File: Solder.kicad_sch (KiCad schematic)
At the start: 83 parts, among them K1 SRD-24VDC-SL-C, U1 5082-7610, U2 5082-7610, U3 5082-7610, X1 1x07F, X2 1x07F, X3 1x07F, X4 1x02, X5 1x04, X6 01x02F

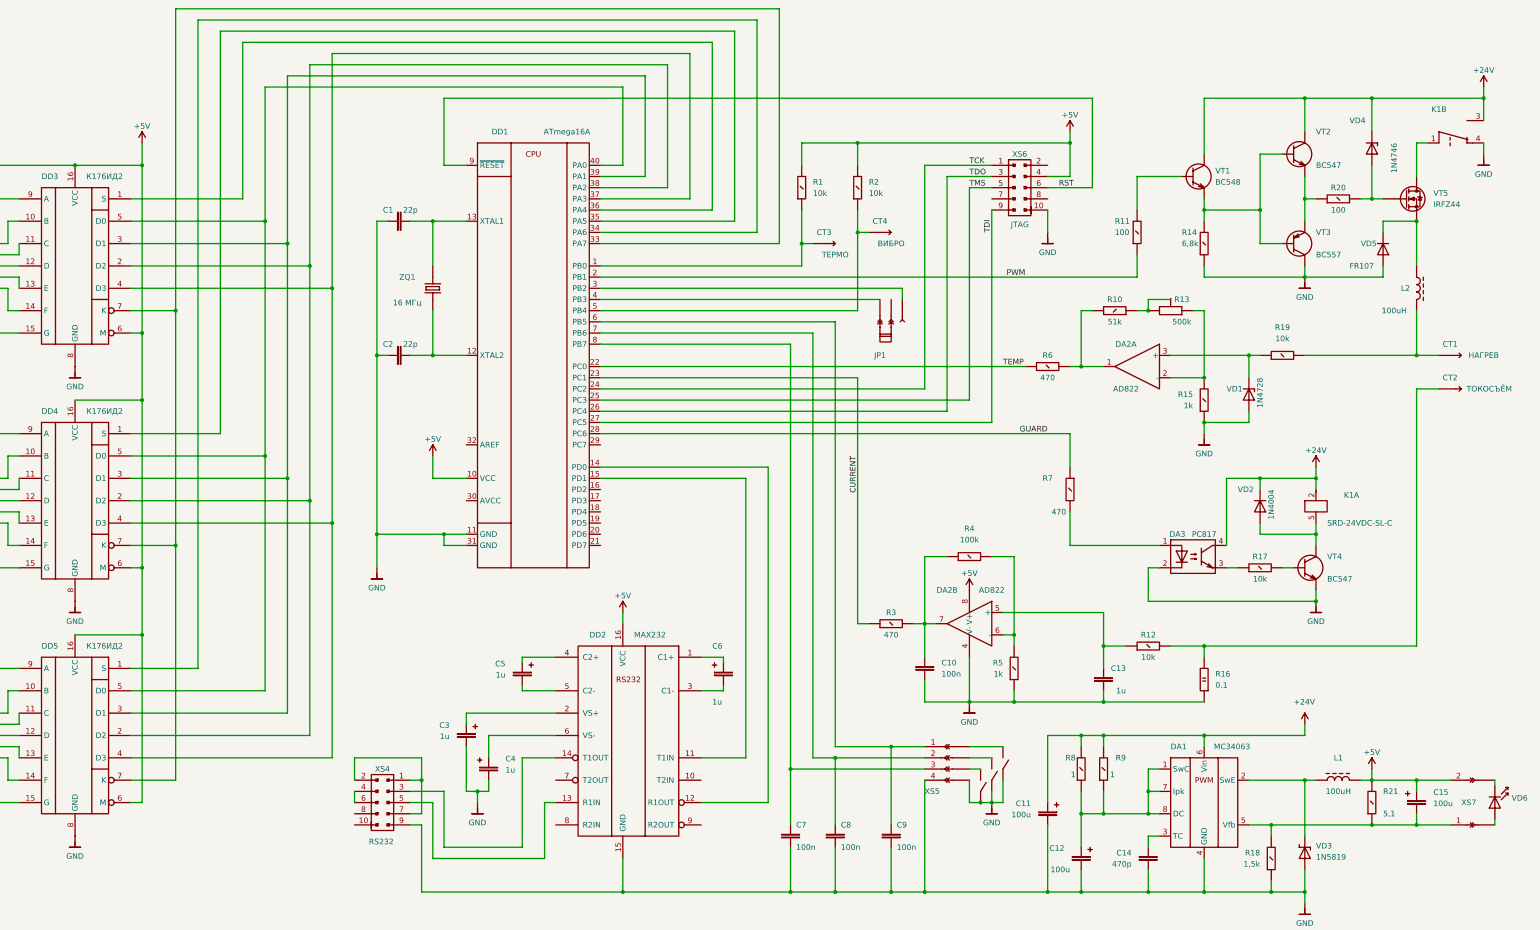
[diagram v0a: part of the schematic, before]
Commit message: Fixed schematic errors
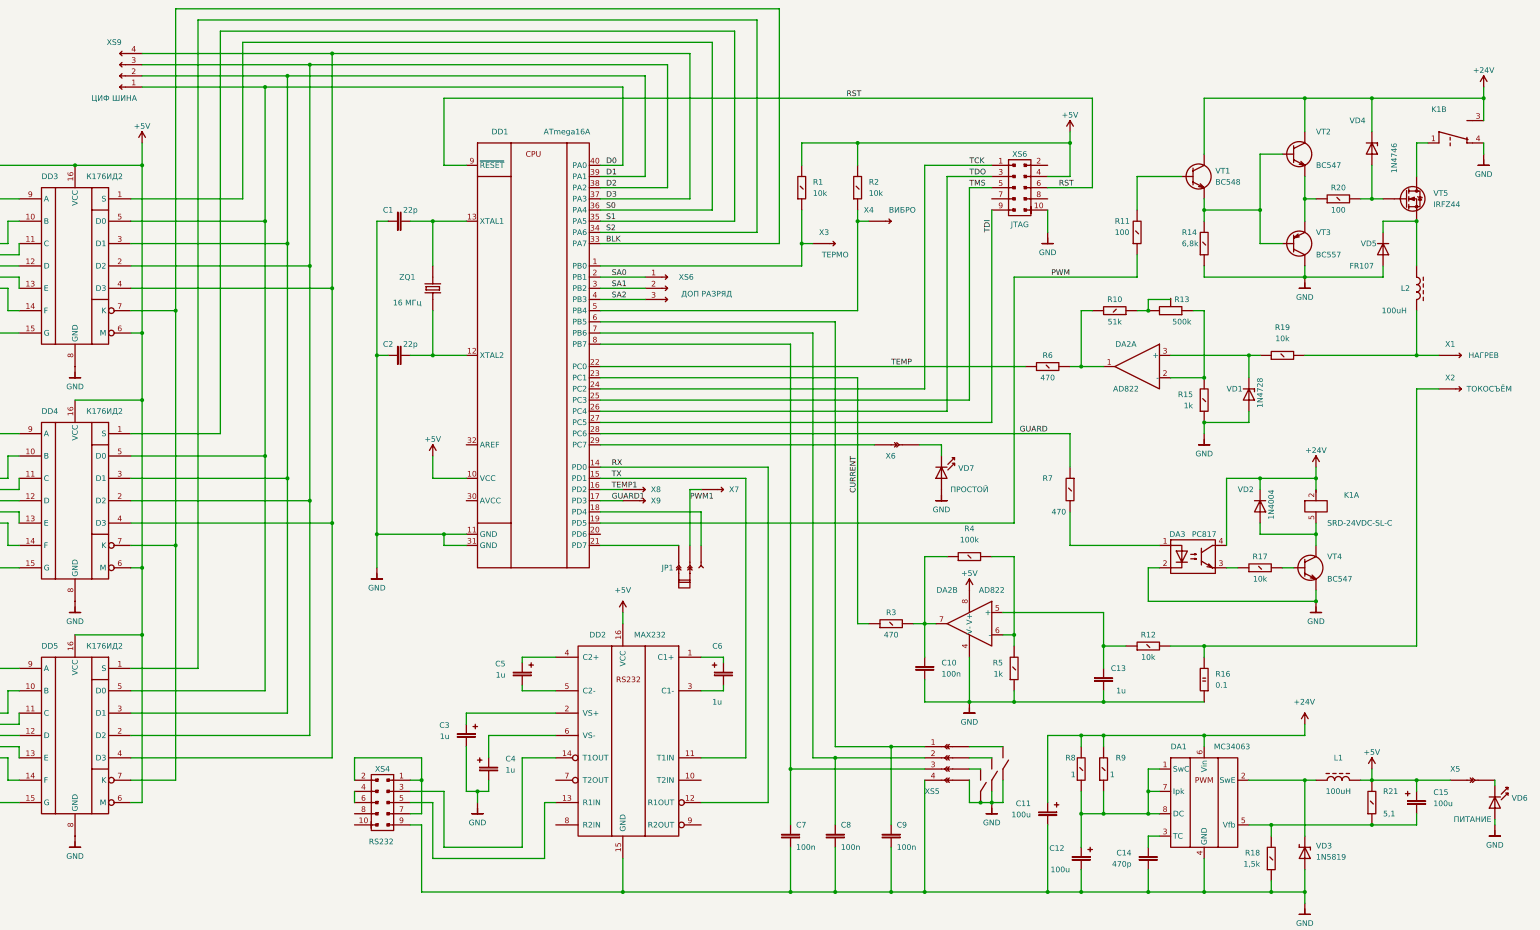
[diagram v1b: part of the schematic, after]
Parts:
- removed X6: 01x02F, Pin Headers:1x02, symbol Pin Headers:1x02F
- removed XS7: 1x02, Pin Headers:1x02, symbol Pin Headers:1x02
- added VD7: ПРОСТОЙ, symbol LEDs:LED
- added X5, X6, X7, X8, X9: 1x01, Pin Headers:Pin, symbol Pin Headers:Pin
- added XP4, XP5: PinF, Pin Headers:Pin, symbol Pin Headers:PinF
- added XS6: ДОП РАЗРЯД, Pin Headers:1x03, symbol Pin Headers:01x03
- added XS9: ЦИФ ШИНА, Pin Headers:1x04, symbol Pin Headers:1x04
- VD6: value LED -> ПИТАНИЕ
- renumbered СТ1 to X1, СТ2 to X2, СТ3 to X3, СТ4 to X4, X1 to XP1, X2 to XP2, X3 to XP3
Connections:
- net +5V: now also X5.1 (Pin_1)
- net GND: now also VD6.2 (A), VD7.2 (A)
- net PWM: now also DD1.19 (PD5); no longer DD1.2 (PB1)
- net at VD6.1 (K): now also XP4.1 (Pin_1)
- net TX: now reaches DD1.15 (PD1), DD2.11 (T1IN)
- net RX: now reaches DD1.14 (PD0), DD2.12 (R1OUT)
- net at JP1.1 (Pin_1): now also DD1.18 (PD4); no longer DD1.3 (PB2)
- net PWM1: now reaches JP1.2 (Pin_2)
- net PWM1: now also X7.1 (Pin_1)
- net at JP1.3 (Pin_3): now also DD1.21 (PD7); no longer DD1.4 (PB3)
- net S0: now reaches DD1.36 (PA4), DD3.1 (S)
- net D2: now reaches DD1.38 (PA2), DD3.2 (D2), DD4.2 (D2), DD5.2 (D2)
- net D2: now also XS9.3 (Pin_3)
- net D1: now reaches DD1.39 (PA1), DD3.3 (D1), DD4.3 (D1), DD5.3 (D1)
- net D1: now also XS9.2 (Pin_2)
- net D3: now reaches DD1.37 (PA3), DD3.4 (D3), DD4.4 (D3), DD5.4 (D3)
- net D3: now also XS9.4 (Pin_4)
- net D0: now reaches DD1.40 (PA0), DD3.5 (D0), DD4.5 (D0), DD5.5 (D0)
- net D0: now also XS9.1 (Pin_1)
- net BLK: now reaches DD1.33 (PA7), DD3.7 (K), DD4.7 (K), DD5.7 (K)
- net S1: now reaches DD1.35 (PA5), DD4.1 (S)
- net TEMP1: now reaches DD1.16 (PD2)
- net TEMP1: now also X8.1 (Pin_1)
- net GUARD1: now reaches DD1.17 (PD3)
- net GUARD1: now also X9.1 (Pin_1)
- net at DD1.29 (PC7): now also X6.1 (Pin_1)
- net S2: now reaches DD1.34 (PA6), DD5.1 (S)
- new net: VD7.1 (K), XP5.1 (Pin_1)
- new net SA0: DD1.2 (PB1), XS6.1 (Pin_1)
- new net SA1: DD1.3 (PB2), XS6.2 (Pin_2)
- new net SA2: DD1.4 (PB3), XS6.3 (Pin_3)
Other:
- moved on the sheet: JP1, X4

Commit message: Routed board
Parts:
- added X10: ПИТАНИЕ, Connectors:PIN-Wire, symbol Pin Headers:PIN-Wire
- added X11: КОРПУС, Connectors:PIN-Wire, symbol Pin Headers:PIN-Wire
- renumbered X4 to JP2, X5 to XP4, XP4 to XP6, XS6 to XS7
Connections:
- net +24V: now also X10.1 (Pin_1)
- net GND: now also XS4.10 (Pin_10), X11.1 (Pin_1)
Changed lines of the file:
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@@
   (junction (at 119.38 83.82) (diameter 0) (color 0 0 0 0)
   )
+  (junction (at 386.08 57.15) (diameter 0) (color 0 0 0 0)
+  )
   (junction (at 294.64 208.28) (diameter 0) (color 0 0 0 0)
   )
@@
   (junction (at 360.68 68.58) (diameter 0) (color 0 0 0 0)
   )
+  (junction (at 144.78 217.17) (diameter 0) (color 0 0 0 0)
+  )
   (junction (at 322.58 119.38) (diameter 0) (color 0 0 0 0)
   )
@@
     (stroke (width 0) (type default))
   )
+  (wire (pts (xy 386.08 57.15) (xy 389.89 57.15))
+    (stroke (width 0) (type default))
+  )
   (wire (pts (xy 345.44 68.58) (xy 347.98 68.58))
     (stroke (width 0) (type default))
@@
     (stroke (width 0) (type default))
   )
+  (wire (pts (xy 386.08 57.15) (xy 386.08 58.42))
+    (stroke (width 0) (type default))
+  )
   (wire (pts (xy 35.56 134.62) (xy 38.1 134.62))
     (stroke (width 0) (type default))
@@
     (stroke (width 0) (type default))
   )
+  (wire (pts (xy 129.54 217.17) (xy 144.78 217.17))
+    (stroke (width 0) (type default))
+  )
   (wire (pts (xy 274.32 149.86) (xy 279.4 149.86))
     (stroke (width 0) (type default))
@@
     (stroke (width 0) (type default))
   )
-  (wire (pts (xy 144.78 210.82) (xy 144.78 226.06))
+  (wire (pts (xy 144.78 210.82) (xy 144.78 217.17))
     (stroke (width 0) (type default))
   )
@@
     (stroke (width 0) (type default))
   )
-  (wire (pts (xy 386.08 55.88) (xy 386.08 58.42))
+  (wire (pts (xy 386.08 55.88) (xy 386.08 57.15))
     (stroke (width 0) (type default))
   )
@@
     (stroke (width 0) (type default))
   )
+  (wire (pts (xy 144.78 217.17) (xy 144.78 226.06))
+    (stroke (width 0) (type default))
+  )
   (wire (pts (xy 299.72 208.28) (xy 309.88 208.28))
     (stroke (width 0) (type default))
@@
     (stroke (width 0) (type default))
   )
+  (wire (pts (xy 129.54 210.82) (xy 129.54 217.17))
+    (stroke (width 0) (type default))
+  )
+  (wire (pts (xy 386.08 45.72) (xy 389.89 45.72))
+    (stroke (width 0) (type default))
+  )
   (wire (pts (xy 81.28 35.56) (xy 124.46 35.56))
     (stroke (width 0) (type default))
@@
     )
   )
-  (symbol (lib_id "Segment:5082-7610") (at 27.94 137.16 0) (unit 1)
+  (symbol (lib_name "5082-7610_2") (lib_id "Segment:5082-7610") (at 27.94 137.16 0) (unit 1)
     (in_bom no) (on_board no) (dnp no) (fields_autoplaced)
     (property "Reference" "U2" (at 27.94 123.19 0)
@@
     )
   )
+  (symbol (lib_id "Pin Headers:PIN-Wire") (at 389.89 57.15 0) (unit 1)
+    (in_bom no) (on_board yes) (dnp no)
+    (property "Reference" "X11" (at 392.43 54.61 0)
+      (effects (font (size 1.27 1.27)))
+    )
+    (property "Value" "КОРПУС" (at 394.97 59.69 0)
+      (effects (font (size 1.27 1.27)))
+    )
+    (property "Footprint" "Connectors:PIN-Wire" (at 393.954 58.674 0)
+      (effects (font (size 1.27 1.27)) hide)
+    )
+    (property "Datasheet" "~" (at 389.89 57.15 0)
+      (effects (font (size 1.27 1.27)) hide)
+    )
+    (property "Sim.Enable" "0" (at 389.89 57.15 0)
+      (effects (font (size 1.27 1.27)) hide)
+    )
+    (pin "1")
+    (instances
+      (project "Solder"
+        (path "/ca4a91a8-f5dc-4004-bc83-2826b7a3bd5e"
+          (reference "X11") (unit 1)
+        )
+      )
+    )
+  )
   (symbol (lib_id "Power:GND") (at 322.58 124.46 0) (unit 1)
     (in_bom yes) (on_board yes) (dnp no)
@@
   (symbol (lib_id "Pin Headers:1x04") (at 264.16 195.58 0) (unit 1)
     (in_bom no) (on_board no) (dnp no) (fields_autoplaced)
-    (property "Reference" "X5" (at 264.795 190.5 0)
+    (property "Reference" "XP4" (at 264.795 190.5 0)
       (effects (font (size 1.27 1.27)) hide)
     )
@@
       (project "Solder"
         (path "/ca4a91a8-f5dc-4004-bc83-2826b7a3bd5e"
-          (reference "X5") (unit 1)
+          (reference "XP4") (unit 1)
         )
       )
@@
   (symbol (lib_id "Pin Headers:Jumper") (at 205.74 152.4 270) (unit 1)
     (in_bom no) (on_board no) (dnp no) (fields_autoplaced)
-    (property "Reference" "X4" (at 207.01 154.6479 90)
+    (property "Reference" "JP2" (at 207.01 154.6479 90)
       (effects (font (size 1.27 1.27)) (justify left) hide)
     )
@@
       (project "Solder"
         (path "/ca4a91a8-f5dc-4004-bc83-2826b7a3bd5e"
-          (reference "X4") (unit 1)
+          (reference "JP2") (unit 1)
         )
       )
@@
     )
   )
+  (symbol (lib_id "Pin Headers:PIN-Wire") (at 389.89 45.72 0) (unit 1)
+    (in_bom no) (on_board yes) (dnp no)
+    (property "Reference" "X10" (at 392.43 43.18 0)
+      (effects (font (size 1.27 1.27)))
+    )
+    (property "Value" "ПИТАНИЕ" (at 394.97 48.26 0)
+      (effects (font (size 1.27 1.27)))
+    )
+    (property "Footprint" "Connectors:PIN-Wire" (at 393.954 47.244 0)
+      (effects (font (size 1.27 1.27)) hide)
+    )
+    (property "Datasheet" "~" (at 389.89 45.72 0)
+      (effects (font (size 1.27 1.27)) hide)
+    )
+    (property "Sim.Enable" "0" (at 389.89 45.72 0)
+      (effects (font (size 1.27 1.27)) hide)
+    )
+    (pin "1")
+    (instances
+      (project "Solder"
+        (path "/ca4a91a8-f5dc-4004-bc83-2826b7a3bd5e"
+          (reference "X10") (unit 1)
+        )
+      )
+    )
+  )
   (symbol (lib_id "Diodes:FR107") (at 363.22 81.28 270) (unit 1)
     (in_bom yes) (on_board yes) (dnp no)
@@
     )
   )
-  (symbol (lib_id "Segment:5082-7610") (at 27.94 83.82 0) (unit 1)
+  (symbol (lib_name "5082-7610_1") (lib_id "Segment:5082-7610") (at 27.94 83.82 0) (unit 1)
     (in_bom no) (on_board no) (dnp no) (fields_autoplaced)
     (property "Reference" "U1" (at 27.94 69.85 0)
@@
   (symbol (lib_id "Pin Headers:01x03") (at 200.66 88.9 0) (mirror y) (unit 1)
     (in_bom yes) (on_board yes) (dnp no)
-    (property "Reference" "XS6" (at 203.2 86.36 0)
+    (property "Reference" "XS7" (at 203.2 86.36 0)
       (effects (font (size 1.27 1.27)) (justify right))
     )
@@
       (project "Solder"
         (path "/ca4a91a8-f5dc-4004-bc83-2826b7a3bd5e"
-          (reference "XS6") (unit 1)
+          (reference "XS7") (unit 1)
         )
       )
@@
   (symbol (lib_id "Pin Headers:PinF") (at 383.54 200.66 180) (unit 1)
     (in_bom no) (on_board no) (dnp no) (fields_autoplaced)
-    (property "Reference" "XP4" (at 384.2131 198.12 0)
+    (property "Reference" "XP6" (at 384.2131 198.12 0)
       (effects (font (size 1.27 1.27)) hide)
     )
@@
       (project "Solder"
         (path "/ca4a91a8-f5dc-4004-bc83-2826b7a3bd5e"
-          (reference "XP4") (unit 1)
+          (reference "XP6") (unit 1)
         )
       )
